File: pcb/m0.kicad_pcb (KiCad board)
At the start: 2 copper layers, 36 x 36 mm, 14 parts, among them U1 SAMD21J

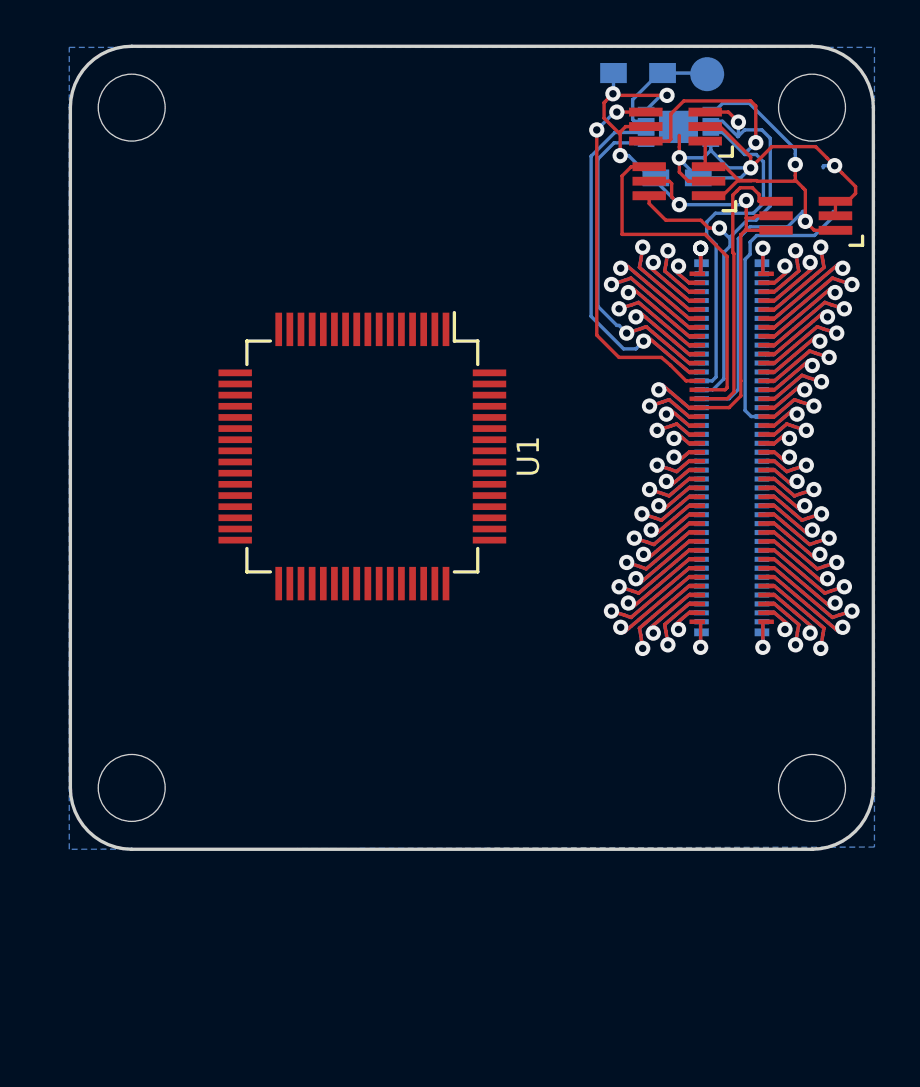
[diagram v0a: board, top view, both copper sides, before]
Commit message: Finished trace routing.
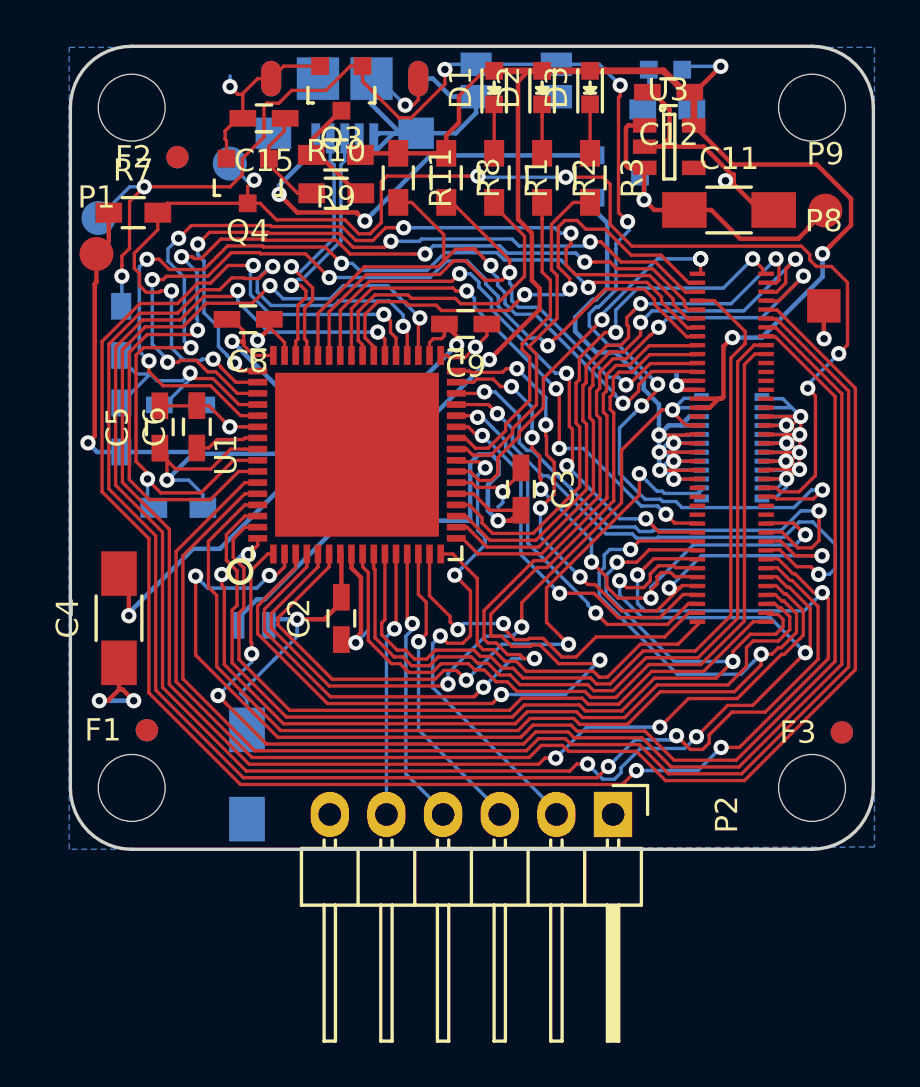
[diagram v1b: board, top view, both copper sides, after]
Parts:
- removed PORT_ANDOR1: SN74LVC1G0832, Housings_SOT-23_SOT-143_TSOT-6:SC-70-6_Handsoldering
- removed PORT_C1: 0.1uF, Capacitors_SMD:C_0603_HandSoldering
- removed PORT_IC1: AT24CS02-MAHM, Housings_DFN_QFN:DFN-8-1EP_3x2mm_Pitch0.5mm
- removed PORT_IN1: CKD_SANDWICH, DF40-80pin-Header
- removed PORT_INV1, PORT_XOR1: SN74LVC1G58, Housings_SOT-23_SOT-143_TSOT-6:SC-70-6_Handsoldering
- removed PORT_P1: CONN_01X01, Measurement_Points:Measurement_Point_Round-SMD-Pad_Small
- removed PORT_R1: 10k, Resistors_SMD:R_0603_HandSoldering
- added C1: 10uF, Capacitors_SMD:C_1206_HandSoldering, B.Cu at (137.9, 122.7)
- added C11: 10uF+, Capacitors_SMD:C_1206_HandSoldering, F.Cu at (159.5, 97.3)
- added C12: 1uF+, Capacitors_SMD:C_0603_HandSoldering, F.Cu at (156.8, 92.1)
- added C15: 2.2uF, Capacitors_SMD:C_0603_HandSoldering, F.Cu at (138.7, 93.2)
- added C2: 0.1uF, Capacitors_SMD:C_0603_HandSoldering, F.Cu at (142.2, 115.7)
- added C3: 0.1uF, Capacitors_SMD:C_0603_HandSoldering, F.Cu at (150.2, 109.8)
- added C4: 10uF, Capacitors_SMD:C_1206_HandSoldering, F.Cu at (132.2, 115.6)
- added C5: 0.1uF, Capacitors_SMD:C_0603_HandSoldering, F.Cu at (134.0, 107.1)
- added C6: 1uF, Capacitors_SMD:C_0603_HandSoldering, F.Cu at (135.7, 107.1)
- added C7: 0.1uF, Capacitors_SMD:C_0603_HandSoldering, B.Cu at (134.9, 106.1)
- added C8: 0.1uF, Capacitors_SMD:C_0603_HandSoldering, F.Cu at (138.0, 102.2)
- added C9: 0.1uF, Capacitors_SMD:C_0603_HandSoldering, F.Cu at (147.7, 102.5)
- added D1: GREEN, LEDs:LED_0603, F.Cu at (149.0, 91.8)
- added D2: YELLOW, LEDs:LED_0603, F.Cu at (151.2, 91.8)
- added D3: RED, LEDs:LED_0603, F.Cu at (153.3, 91.8)
- added D4: D_Schottky_x2_KCom_AAK, TO_SOT_Packages_SMD:SOT-23, B.Cu at (154.5, 95.8)
- added D5: Red, LEDs:LED_0603, B.Cu at (156.7, 91.0)
- added F1: 1mm, macrofab:Fiducial, F.Cu at (133.4, 120.7)
- added F2: 1mm, macrofab:Fiducial, F.Cu at (134.8, 95.0)
- added F3: 1mm, macrofab:Fiducial, F.Cu at (164.6, 120.8)
- added F4: 1mm, macrofab:Fiducial, B.Cu at (133.4, 120.7)
- added F5: 1mm, macrofab:Fiducial, B.Cu at (134.8, 95.0)
- added F6: 1mm, macrofab:Fiducial, B.Cu at (164.6, 120.8)
- added L1: INDUCTOR_SMALL, Inductors_NEOSID:Neosid_Inductor_SM0603CG, B.Cu at (138.2, 116.0)
- added P1: 3V3, Measurement_Points:Measurement_Point_Round-SMD-Pad_Small, F.Cu at (131.2, 99.3)
- added P2: CONN_01X06, Pin_Headers:Pin_Header_Angled_1x06, F.Cu at (154.3, 124.4)
- added P3: USB_OTG, fci:Mini-USB-B-EDGE, B.Cu at (142.3, 92.7)
- added P5: CONN_02X10, hirose-df40:DF40-20pin-Header, B.Cu at (159.7, 108.0)
- added P6: RESET, Measurement_Points:Measurement_Point_Round-SMD-Pad_Small, B.Cu at (131.3, 97.7)
- added P7: BOOT0, Measurement_Points:Measurement_Point_Round-SMD-Pad_Small, B.Cu at (137.2, 95.3)
- added P8: CONN_01X01, Measurement_Points:Measurement_Point_Square-SMD-Pad_Small, F.Cu at (163.8, 101.6)
- added P9: 5V, Measurement_Points:Measurement_Point_Round-SMD-Pad_Small, F.Cu at (163.8, 97.4)
- added Q3: Q_NMOS_GSD, TO_SOT_Packages_SMD:SOT-23, F.Cu at (142.2, 91.9)
- added Q4: Q_NMOS_GSD, TO_SOT_Packages_SMD:SOT-23, F.Cu at (137.9, 96.0)
- added R1: 1k, Resistors_SMD:R_0603_HandSoldering, F.Cu at (149.0, 95.9)
- added R10: 100k, Resistors_SMD:R_0603_HandSoldering, F.Cu at (141.9, 96.6)
- added R11: 2k, Resistors_SMD:R_0603_HandSoldering, F.Cu at (144.7, 95.9)
- added R12: 1k, Resistors_SMD:R_0603_HandSoldering, B.Cu at (156.8, 92.8)
- added R2: 1k, Resistors_SMD:R_0603_HandSoldering, F.Cu at (151.2, 95.9)
- added R3: 1k, Resistors_SMD:R_0603_HandSoldering, F.Cu at (153.3, 95.9)
- added R4: 1k, Resistors_SMD:R_0603_HandSoldering, B.Cu at (134.8, 110.7)
- added R5: 330, Resistors_SMD:R_0603_HandSoldering, B.Cu at (132.3, 102.8)
- added R6: 10k, Resistors_SMD:R_0603_HandSoldering, B.Cu at (132.3, 107.1)
- added R7: 10k, Resistors_SMD:R_0603_HandSoldering, F.Cu at (132.8, 97.5)
- added R8: 2k, Resistors_SMD:R_0603_HandSoldering, F.Cu at (146.8, 95.9)
- added R9: 470k, Resistors_SMD:R_0603_HandSoldering, F.Cu at (141.9, 94.9)
- added SW1: SW_PUSH, Buttons_Switches_SMD:SW_SPST_EVQP7A, B.Cu at (150.0, 91.5)
- added U3: TLV70233DBV, TO_SOT_Packages_SMD:SOT-23-5, F.Cu at (156.8, 94.5)
- PORT_OUT1: value DF40-3-4mm-80pin-Receptacle -> CKD_SANDWICH
- U1: footprint Housings_QFP:TQFP-64_10x10mm_Pitch0.5mm -> Housings_DFN_QFN:QFN-64-1EP_9x9mm_Pitch0.5mm
- moved U1 0.25 mm to (142.9, 108.3), turned to 90 degrees
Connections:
- PORT_OUT1 pad 1: (no net) -> /TIM1
- PORT_OUT1 pad 10: (no net) -> /GPIO6
- PORT_OUT1 pad 11: (no net) -> /i2c_SDA
- PORT_OUT1 pad 12: (no net) -> /i2c_SCL
- PORT_OUT1 pad 13: (no net) -> GND
- PORT_OUT1 pad 14: (no net) -> GND
- PORT_OUT1 pad 15: (no net) -> VDD
- PORT_OUT1 pad 16: (no net) -> VDD
- PORT_OUT1 pad 17: (no net) -> Net-(PORT_OUT1-Pad17)
- PORT_OUT1 pad 18: (no net) -> +BATT
- PORT_OUT1 pad 19: (no net) -> +5V
- PORT_OUT1 pad 2: (no net) -> /TIM2
- PORT_OUT1 pad 20: (no net) -> +5V
- PORT_OUT1 pad 21: (no net) -> +5V
- PORT_OUT1 pad 22: (no net) -> +5V
- PORT_OUT1 pad 23: (no net) -> +5V
- PORT_OUT1 pad 24: (no net) -> +5V
- PORT_OUT1 pad 25: (no net) -> Net-(PORT_OUT1-Pad25)
- PORT_OUT1 pad 26: (no net) -> Net-(PORT_OUT1-Pad26)
- PORT_OUT1 pad 27: (no net) -> Net-(PORT_OUT1-Pad27)
- PORT_OUT1 pad 28: (no net) -> Net-(PORT_OUT1-Pad28)
- PORT_OUT1 pad 29: (no net) -> /UART6_TX
- PORT_OUT1 pad 3: (no net) -> /TIM3
- PORT_OUT1 pad 30: (no net) -> /UART6_RX
- PORT_OUT1 pad 31: (no net) -> /UART5_TX_SPI1_NSS
- PORT_OUT1 pad 32: (no net) -> /UART5_RX_SPI1_MISO
- PORT_OUT1 pad 33: (no net) -> /UART4_TX_SPI2_NSS
- PORT_OUT1 pad 34: (no net) -> /UART4_RX_SPI2_MISO
- PORT_OUT1 pad 35: (no net) -> /UART3_TX_SPI3_NSS
- PORT_OUT1 pad 36: (no net) -> /UART3_RX_SPI3_MISO
- PORT_OUT1 pad 37: (no net) -> /UART2_TX
- PORT_OUT1 pad 38: (no net) -> /UART2_RX
- PORT_OUT1 pad 39: (no net) -> /UART1_TX
- PORT_OUT1 pad 4: (no net) -> /TIM4
- PORT_OUT1 pad 40: (no net) -> /UART1_RX
- PORT_OUT1 pad 41: (no net) -> /TIMG1_CH1
- PORT_OUT1 pad 42: (no net) -> /TIMG1_CH2
- PORT_OUT1 pad 43: (no net) -> /TIMG1_CH3
- PORT_OUT1 pad 44: (no net) -> /TIMG1_CH4
- PORT_OUT1 pad 45: (no net) -> /TIMG2_CH1
- PORT_OUT1 pad 46: (no net) -> /TIMG2_CH2
- PORT_OUT1 pad 47: (no net) -> /TIMG2_CH3
- PORT_OUT1 pad 48: (no net) -> /TIMG2_CH4
- PORT_OUT1 pad 49: (no net) -> /ADC1
- PORT_OUT1 pad 5: (no net) -> /GPIO1
- PORT_OUT1 pad 50: (no net) -> /ADC2
- PORT_OUT1 pad 51: (no net) -> Net-(PORT_OUT1-Pad51)
- PORT_OUT1 pad 52: (no net) -> Net-(PORT_OUT1-Pad52)
- PORT_OUT1 pad 53: (no net) -> Net-(PORT_OUT1-Pad53)
- PORT_OUT1 pad 54: (no net) -> Net-(PORT_OUT1-Pad54)
- PORT_OUT1 pad 55: (no net) -> Net-(PORT_OUT1-Pad55)
- PORT_OUT1 pad 56: (no net) -> Net-(PORT_OUT1-Pad56)
- PORT_OUT1 pad 57: (no net) -> GND
- PORT_OUT1 pad 58: (no net) -> GND
- PORT_OUT1 pad 59: (no net) -> GND
- PORT_OUT1 pad 6: (no net) -> /GPIO2
- PORT_OUT1 pad 60: (no net) -> GND
- PORT_OUT1 pad 61: (no net) -> GND
- PORT_OUT1 pad 62: (no net) -> GND
- PORT_OUT1 pad 63: (no net) -> GND
- PORT_OUT1 pad 64: (no net) -> GND
- PORT_OUT1 pad 65: (no net) -> /Reset/BOOT0
- PORT_OUT1 pad 66: (no net) -> /Reset/RESET
- PORT_OUT1 pad 67: (no net) -> Net-(PORT_OUT1-Pad67)
- PORT_OUT1 pad 68: (no net) -> Net-(PORT_OUT1-Pad68)
- PORT_OUT1 pad 69: (no net) -> /UART3_TX_SPI3_NSS
- PORT_OUT1 pad 7: (no net) -> /GPIO3
- PORT_OUT1 pad 70: (no net) -> /SPI3_SCK
- PORT_OUT1 pad 71: (no net) -> /UART3_RX_SPI3_MISO
- PORT_OUT1 pad 72: (no net) -> /SPI3_MOSI
- PORT_OUT1 pad 73: (no net) -> /UART4_TX_SPI2_NSS
- PORT_OUT1 pad 74: (no net) -> /SPI2_SCK
- PORT_OUT1 pad 75: (no net) -> /UART4_RX_SPI2_MISO
- PORT_OUT1 pad 76: (no net) -> /SPI2_MOSI
- PORT_OUT1 pad 77: (no net) -> /UART5_TX_SPI1_NSS
- PORT_OUT1 pad 78: (no net) -> /SPI1_SCK
- PORT_OUT1 pad 79: (no net) -> /UART5_RX_SPI1_MISO
- PORT_OUT1 pad 8: (no net) -> /GPIO4
- PORT_OUT1 pad 80: (no net) -> /SPI1_MOSI
- PORT_OUT1 pad 9: (no net) -> /GPIO5
- U1 pad 10: /ADC2 -> /ADC1
- U1 pad 12: Net-(U1-Pad12) -> /D3
- U1 pad 13: Net-(U1-Pad13) -> /D2
- U1 pad 14: Net-(U1-Pad14) -> /D1
- U1 pad 17: /TIMG1_CH1 -> /TIMG1_CH4
- U1 pad 18: /TIMG1_CH2 -> /TIMG1_CH3
- U1 pad 19: /TIMG1_CH3 -> /TIMG1_CH2
- U1 pad 20: /TIMG1_CH4 -> /TIMG1_CH1
- U1 pad 21: Net-(U1-Pad21) -> VDD
- U1 pad 22: Net-(U1-Pad22) -> GND
- U1 pad 24: Net-(U1-Pad24) -> /D0
- U1 pad 25: Net-(U1-Pad25) -> /LED3
- U1 pad 26: Net-(U1-Pad26) -> /LED2
- U1 pad 3: /GPIO5 -> /GPIO6
- U1 pad 33: Net-(U1-Pad33) -> GND
- U1 pad 34: Net-(U1-Pad34) -> VDD
- U1 pad 4: /GPIO6 -> /GPIO5
- U1 pad 40: Net-(U1-Pad40) -> /LED1
- U1 pad 45: Net-(U1-Pad45) -> /USB-
- U1 pad 46: Net-(U1-Pad46) -> /USB+
- U1 pad 47: Net-(U1-Pad47) -> GND
- U1 pad 48: Net-(U1-Pad48) -> VDD
- U1 pad 5: /+BATT -> +BATT
- U1 pad 50: Net-(U1-Pad50) -> /Reset/BOOT0
- U1 pad 54: Net-(U1-Pad54) -> GND
- U1 pad 56: Net-(U1-Pad56) -> VDD
- U1 pad 6: Net-(U1-Pad6) -> /Power/CURRENT
- U1 pad 8: Net-(U1-Pad8) -> GND
- U1 pad 9: /ADC1 -> /ADC2
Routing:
- net VDD: track 0.00 -> 167.4 mm, vias 0 -> 10
- net GND: track 0.00 -> 102.7 mm, vias 0 -> 20
- net /UART4_TX_SPI2_NSS: track 16.0 -> 88.3 mm, vias 2 -> 6
- net /Reset/RESET: track 0.00 -> 70.0 mm, vias 0 -> 8
- net /SPI2_SCK: track 9.44 -> 75.4 mm, vias 1 -> 4
- net GNDPWR: track 65.6 -> 0.00 mm, vias 11 -> 0
- net /UART4_RX_SPI2_MISO: track 18.3 -> 83.4 mm, vias 2 -> 6
- net /Reset/BOOT0: track 0.00 -> 64.2 mm, vias 0 -> 7
- net /SPI2_MOSI: track 8.44 -> 68.7 mm, vias 1 -> 4
- net /TIMG2_CH1: track 8.44 -> 63.7 mm, vias 1 -> 0
- net /TIMG2_CH2: track 8.88 -> 61.5 mm, vias 1 -> 0
- net /TIMG2_CH4: track 7.98 -> 57.7 mm, vias 1 -> 2
- net /TIMG2_CH3: track 9.44 -> 56.0 mm, vias 1 -> 2
- net /UART5_TX_SPI1_NSS: track 13.0 -> 56.2 mm
- net /GPIO2: track 8.88 -> 48.3 mm, vias 1 -> 5
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- added copper zone on B.Cu, net GND
- removed copper zone on B.Cu, net GNDPWR
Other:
- net class Default: clearance 0.1524 -> 0.14986
- rule trace_clearance: 0.1524 -> 0.14986
- rule trace_min: 0.1524 -> 0.006
- rule via_min_size: 0.6858 -> 0.013

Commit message: Add license information to many files. PCB design files are CC-BY and code is MIT license.
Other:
- board text added: "Copyright 2016 Chickadee Tech LLC, <add attributions here> This work is licensed under the Creative Commons Attribution 4.0 International License. To view a copy of this license, visit http://creativecommons.org/licenses/by/4.0/ or send a letter to Creative Commons, PO Box 1866, Mountain View, CA 94042, USA."
- board text added: "Remove all Chickadee Tech LLC trademarks before making your own board. The Chickadee logo and Polystack logo are owned by Chickadee Tech LLC. You may license the Polystack logo for free by emailing support@chickadee.tech and receiving express written permission from Chickadee Tech LLC."
- board text added: "The gear logo is a mark designating open source hardware. Remove it if your design does not comply with the open source hardware definition."
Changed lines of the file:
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@@
     (area 118.127143 74.1 205.267857 178)
     (thickness 1.6)
-    (drawings 26)
+    (drawings 29)
     (tracks 1950)
     (zones 0)
@@
     (40 Dwgs.User user)
     (41 Cmts.User user)
-    (42 Eco1.User user hide)
+    (42 Eco1.User user)
     (43 Eco2.User user)
     (44 Edge.Cuts user)
@@
       (solder_mask_margin 0.5) (solder_paste_margin_ratio -0.5) (clearance 0.5))
   )
+  (gr_text "The gear logo is a mark designating open\nsource hardware. Remove it if your design\ndoes not comply with the open source\nhardware definition." (at 163.54 134.4) (layer Cmts.User)
+    (effects (font (size 1.5 1.5) (thickness 0.3)) (justify left))
+  )
+  (gr_text "Remove all Chickadee Tech LLC trademarks\nbefore making your own board. The\nChickadee logo and Polystack logo\nare owned by Chickadee Tech LLC.\n\nYou may license the Polystack logo for\nfree by emailing support@chickadee.tech\nand receiving express written permission\nfrom Chickadee Tech LLC." (at 60.01 109.71) (layer Cmts.User)
+    (effects (font (size 1.5 1.5) (thickness 0.3)) (justify left))
+  )
+  (gr_text "Copyright 2016 Chickadee Tech LLC, <add attributions here>\n\nThis work is licensed under the Creative Commons Attribution 4.0 International License.\nTo view a copy of this license, visit http://creativecommons.org/licenses/by/4.0/\nor send a letter to Creative Commons, PO Box 1866, Mountain View, CA 94042, USA." (at 179.03 173.78) (layer Cmts.User)
+    (effects (font (size 1.5 1.5) (thickness 0.3)) (justify left))
+  )
   (gr_circle (center 137.6 113.55) (end 138 113.86) (layer F.SilkS) (width 0.2))
   (gr_text "Try to keep components outside\nthe yellow rings. They designate\n8mm diameter washers that may\nbe used to separate boards." (at 167.5 100.9) (layer Eco2.User)
@@
   (gr_line (start 166 92.75) (end 166 123.25) (angle 90) (layer Edge.Cuts) (width 0.15))
   (gr_line (start 132.75 90) (end 163.25 90) (angle 90) (layer Edge.Cuts) (width 0.15))
-  (gr_text m0 (at 187.25 174.25) (layer Cmts.User)
-    (effects (font (size 5 5) (thickness 0.5)) (justify left))
+  (gr_text m0 (at 186.92 189.78) (layer Cmts.User)
+    (effects (font (size 3 3) (thickness 0.5)) (justify left))
   )
   (segment (start 138.40125 111.56125) (end 137.82385 111.56125) (width 0.1524) (layer F.Cu) (net 1))
